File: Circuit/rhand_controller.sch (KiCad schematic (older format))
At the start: 5 parts

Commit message: 回路図ほぼ完成
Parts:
- added C?: C, symbol C
- added P?: V_ADC, symbol CONN_01X03
- added P?: W_ADC, symbol CONN_01X03
- added P?: U_ADC, symbol CONN_01X03
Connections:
- net +3V3: now also P?.2 (3.3V), P?.4 (3.3V), C?.1, P?.3 (P3), P?.3 (P3), P?.3 (P3)
- net GND: now also P?.1 (GND), P?.5 (GND), C?.2, P?.1 (P1), P?.1 (P1), P?.1 (P1)
- net U: now reaches U?.10 (PA4/SPI1_NSS/I2S1_WS/TIM14_CH1/TSC_G2_IO1/USART2_CK/USB_NOE/ADC_IN4)
- net U: now also P?.2 (P2)
- net V: now reaches U?.11 (PA5/SPI1_SCK/I2S1_CK/CEC/TIM2_CH1_ETR/TSC_G2_IO2/ADC_IN5)
- net V: now also P?.2 (P2)
- net W: now reaches U?.12 (PA6/SPI1_MISO/I2S1_MCK/TIM3_CH1/TIM1_BKIN/TIM16_CH1/TSC_G2_IO3/EVENTOUT/ADC_IN6)
- net W: now also P?.2 (P2)
- net RSW_B0: now reaches U?.13 (PA7/SPI1_MOSI/I2S1_SD/TIM3_CH2/TIM14_CH1/TIM1_CH1N/TIM17_CH1/TSC_G2_IO4/EVENTOUT/ADC_IN7)
- net RSW_B1: now reaches U?.18 (PA8/USART1_CK/TIM1_CH1/EVENTOUT/MCO/CRS_SYNC)
- net RSW_B2: now reaches U?.19 (PA9/USART1_TX/TIM1_CH2/TSC_G4_IO1/I2C1_SCL)
- net RSW_B3: now reaches U?.20 (PA10/USART1_RX/TIM1_CH3/TIM17_BKIN/TSC_G4_IO2/I2C1_SDA)
- net Blutooth_RXD: now reaches U?.29 (PB6/I2C1_SCL/USART1_TX/TIM16_CH1N/TSC_G5_IO4)
- net Blutooth_RXD: now also P?.8 (RXD)
- net Blutooth_TXD: now reaches U?.30 (PB7/I2C1_SDA/USART1_RX/TIM17_CH1N/TSC_G5_IO4)
- net Blutooth_TXD: now also P?.7 (TXD)
- net 315MHz_RXD: now reaches U?.8 (PA2/USART2_TX/TIM2_CH3/TSC_G1_IO3/ADC_IN2)
- net 315MHz_TXD: now reaches U?.9 (PA3/USART2_RX/TIM2_CH4/TSC_G1_IO4/ADC_IN3)
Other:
- moved on the sheet: P?

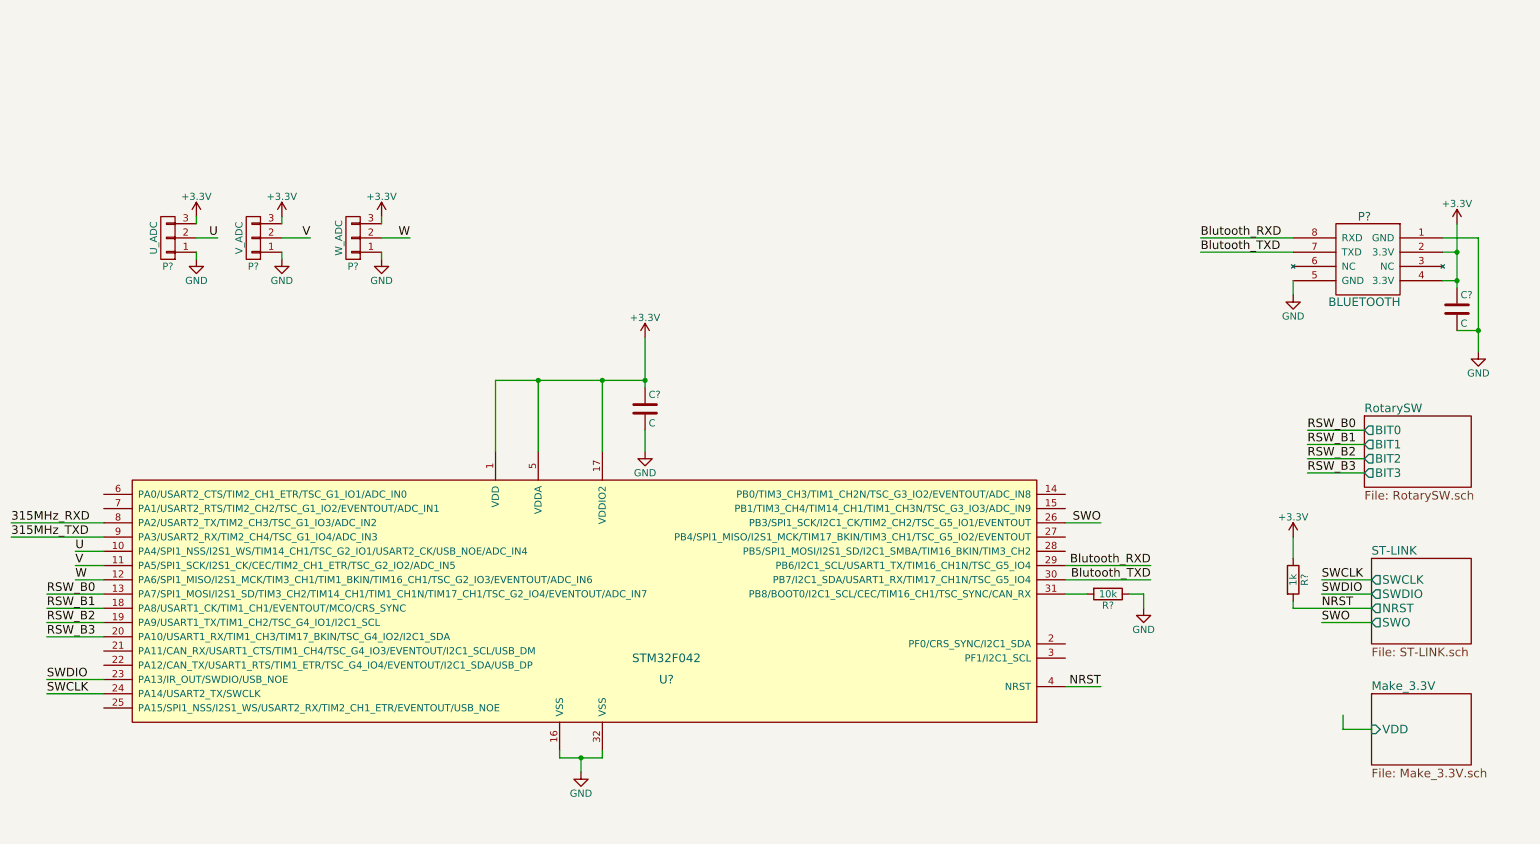
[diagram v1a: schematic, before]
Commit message: 315MHzモジュールなどの追加
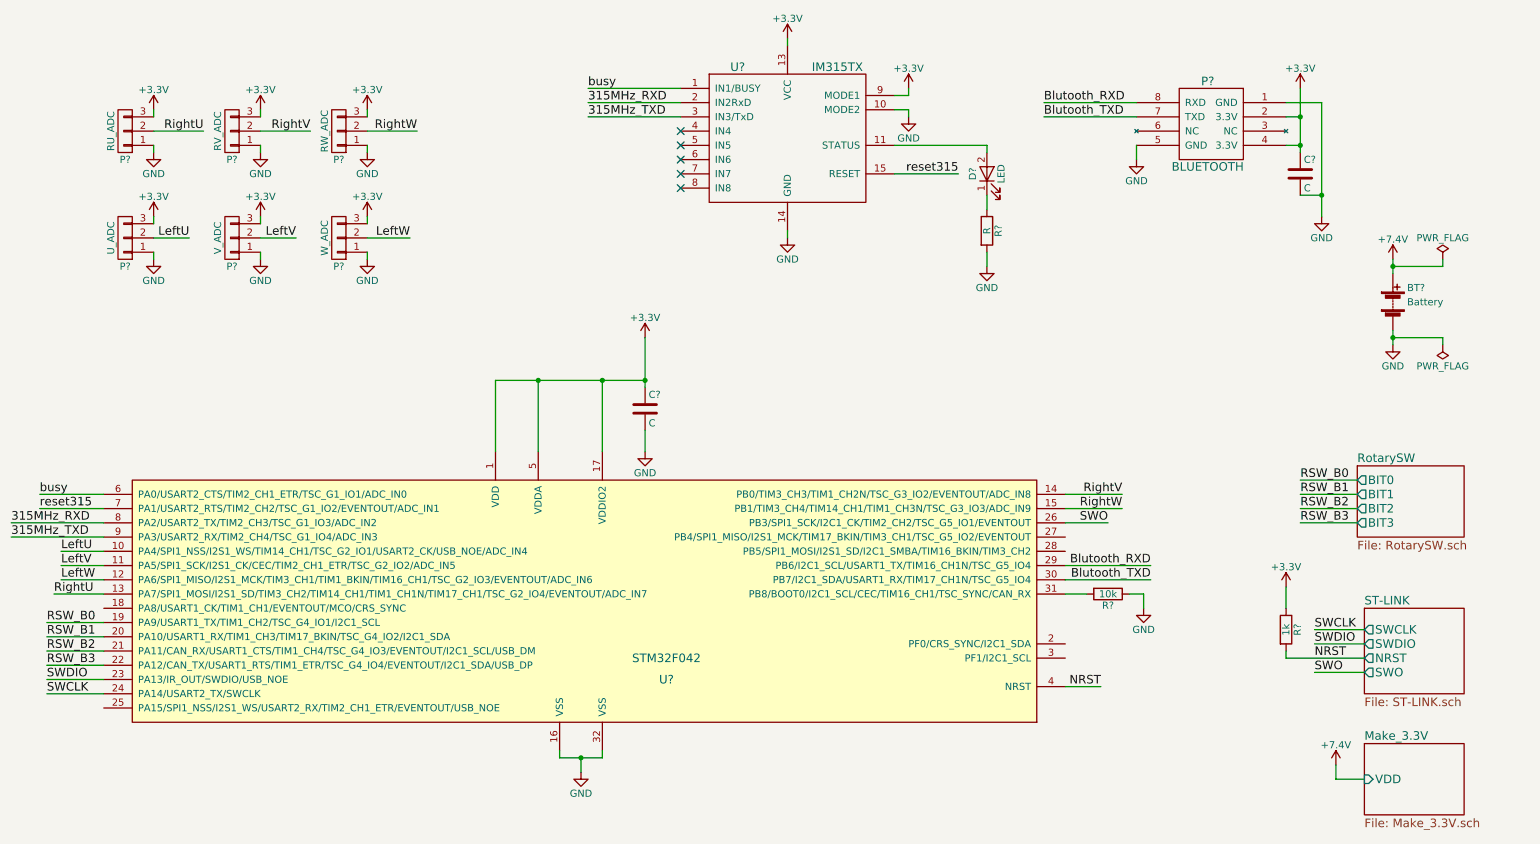
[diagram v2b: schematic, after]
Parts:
- added BT?: Battery, symbol Battery
- added D?: LED, symbol LED
- added P?: V_ADC, symbol CONN_01X03
- added P?: W_ADC, symbol CONN_01X03
- added P?: U_ADC, symbol CONN_01X03
- added R?: R, symbol R
- added U?: IM315TX, symbol IM315TX
- P?: value V_ADC -> RV_ADC
- P?: value W_ADC -> RW_ADC
- P?: value U_ADC -> RU_ADC
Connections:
- net +3V3: now also P?.3 (P3), P?.3 (P3), P?.3 (P3), U?.13 (VCC), U?.9 (MODE1)
- net 315MHz_RXD: now also U?.2 (IN2RxD)
- net 315MHz_TXD: now also U?.3 (IN3/TxD)
- net GND: now also BT?.2 (-), P?.1 (P1), P?.1 (P1), P?.1 (P1), R?.2, U?.10 (MODE2), U?.14 (GND)
- net RSW_B0: now also U?.19 (PA9/USART1_TX/TIM1_CH2/TSC_G4_IO1/I2C1_SCL); no longer U?.13 (PA7/SPI1_MOSI/I2S1_SD/TIM3_CH2/TIM14_CH1/TIM1_CH1N/TIM17_CH1/TSC_G2_IO4/EVENTOUT/ADC_IN7)
- net RSW_B1: now also U?.20 (PA10/USART1_RX/TIM1_CH3/TIM17_BKIN/TSC_G4_IO2/I2C1_SDA); no longer U?.18 (PA8/USART1_CK/TIM1_CH1/EVENTOUT/MCO/CRS_SYNC)
- net RSW_B2: now also U?.21 (PA11/CAN_RX/USART1_CTS/TIM1_CH4/TSC_G4_IO3/EVENTOUT/I2C1_SCL/USB_DM); no longer U?.19 (PA9/USART1_TX/TIM1_CH2/TSC_G4_IO1/I2C1_SCL)
- net RSW_B3: now also U?.22 (PA12/CAN_TX/USART1_RTS/TIM1_ETR/TSC_G4_IO4/EVENTOUT/I2C1_SDA/USB_DP); no longer U?.20 (PA10/USART1_RX/TIM1_CH3/TIM17_BKIN/TSC_G4_IO2/I2C1_SDA)
- net RightV: now reaches U?.14 (PB0/TIM3_CH3/TIM1_CH2N/TSC_G3_IO2/EVENTOUT/ADC_IN8)
- net RightV: now also P?.2 (P2)
- net RightW: now reaches U?.15 (PB1/TIM3_CH4/TIM14_CH1/TIM1_CH3N/TSC_G3_IO3/ADC_IN9)
- net RightW: now also P?.2 (P2)
- net busy: now reaches U?.6 (PA0/USART2_CTS/TIM2_CH1_ETR/TSC_G1_IO1/ADC_IN0)
- net busy: now also U?.1 (IN1/BUSY)
- net reset315: now reaches U?.7 (PA1/USART2_RTS/TIM2_CH2/TSC_G1_IO2/EVENTOUT/ADC_IN1)
- net reset315: now also U?.15 (RESET)
- net U renamed LeftU
- net LeftU: now also P?.2 (P2); no longer P?.2 (P2)
- net V renamed LeftV
- net LeftV: now also P?.2 (P2); no longer P?.2 (P2)
- net W renamed LeftW
- net LeftW: now also P?.2 (P2); no longer P?.2 (P2)
- new net: D?.2 (A), U?.11 (STATUS)
- new net: D?.1 (K), R?.1
- new net +7.4V: BT?.1 (+)
- new net RightU: P?.2 (P2), U?.13 (PA7/SPI1_MOSI/I2S1_SD/TIM3_CH2/TIM14_CH1/TIM1_CH1N/TIM17_CH1/TSC_G2_IO4/EVENTOUT/ADC_IN7)
- no-connect marks 0 -> 5
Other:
- moved on the sheet: C?, P?, R?
